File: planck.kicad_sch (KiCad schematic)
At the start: 142 parts, among them J1 USB_C_U262-161N-4BVC11, J2 USB_C_U262-161N-4BVC11, J3 USB_C_U262-161N-4BVC11, SW1 SW_Hotswap_Kailh_Choc_V1_1u, SW10 SW_Hotswap_Kailh_Choc_V1_1u, SW11 SW_Hotswap_Kailh_Choc_V1_1u, SW12 SW_Hotswap_Kailh_Choc_V1_1u, SW13 SW_Hotswap_Kailh_Choc_V1_1u, SW14 SW_Hotswap_Kailh_Choc_V1_1u, SW15 SW_Hotswap_Kailh_Choc_V1_1u, SW16 SW_Hotswap_Kailh_Choc_V1_1u, SW17 SW_Hotswap_Kailh_Choc_V1_1u, SW18 SW_Hotswap_Kailh_Choc_V1_1u, SW19 SW_Hotswap_Kailh_Choc_V1_1u, SW2 SW_Hotswap_Kailh_Choc_V1_1u, SW20 SW_Hotswap_Kailh_Choc_V1_1u, SW21 SW_Hotswap_Kailh_Choc_V1_1u, SW22 SW_Hotswap_Kailh_Choc_V1_1u, SW23 SW_Hotswap_Kailh_Choc_V1_1u, SW24 SW_Hotswap_Kailh_Choc_V1_1u, SW25 SW_Push, SW26 DSHP02TSGET, SW3 SW_Hotswap_Kailh_Choc_V1_1u, SW4 SW_Hotswap_Kailh_Choc_V1_1u, SW5 SW_Hotswap_Kailh_Choc_V1_1u, SW6 SW_Hotswap_Kailh_Choc_V1_1u, SW7 SW_Hotswap_Kailh_Choc_V1_1u, SW8 SW_Hotswap_Kailh_Choc_V1_1u, SW9 SW_Hotswap_Kailh_Choc_V1_1u, U1 RP2040 ARM Cortex-M0 133MHz, U2 ME6219C33M5G, U3 W25Q16JVUXIQ, U5 tcase, Y1 32MHz ±10ppm 20pF SMD3225-4P

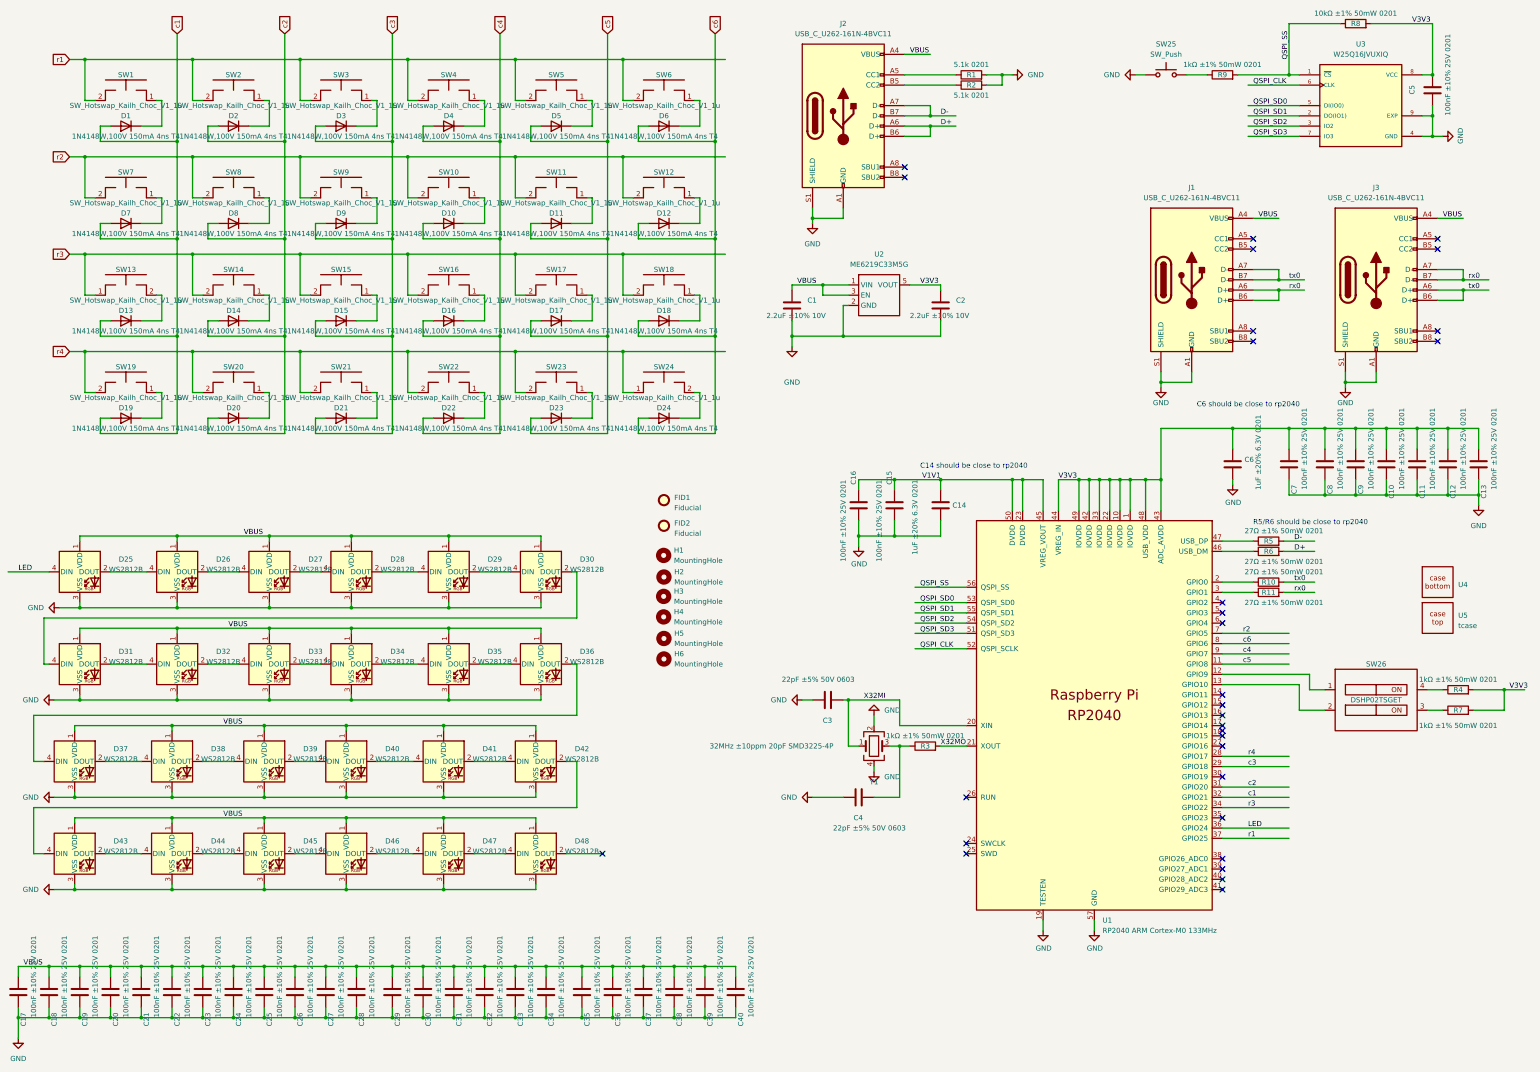
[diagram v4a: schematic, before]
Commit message: little  layout modification resistor over serial for protection  27R
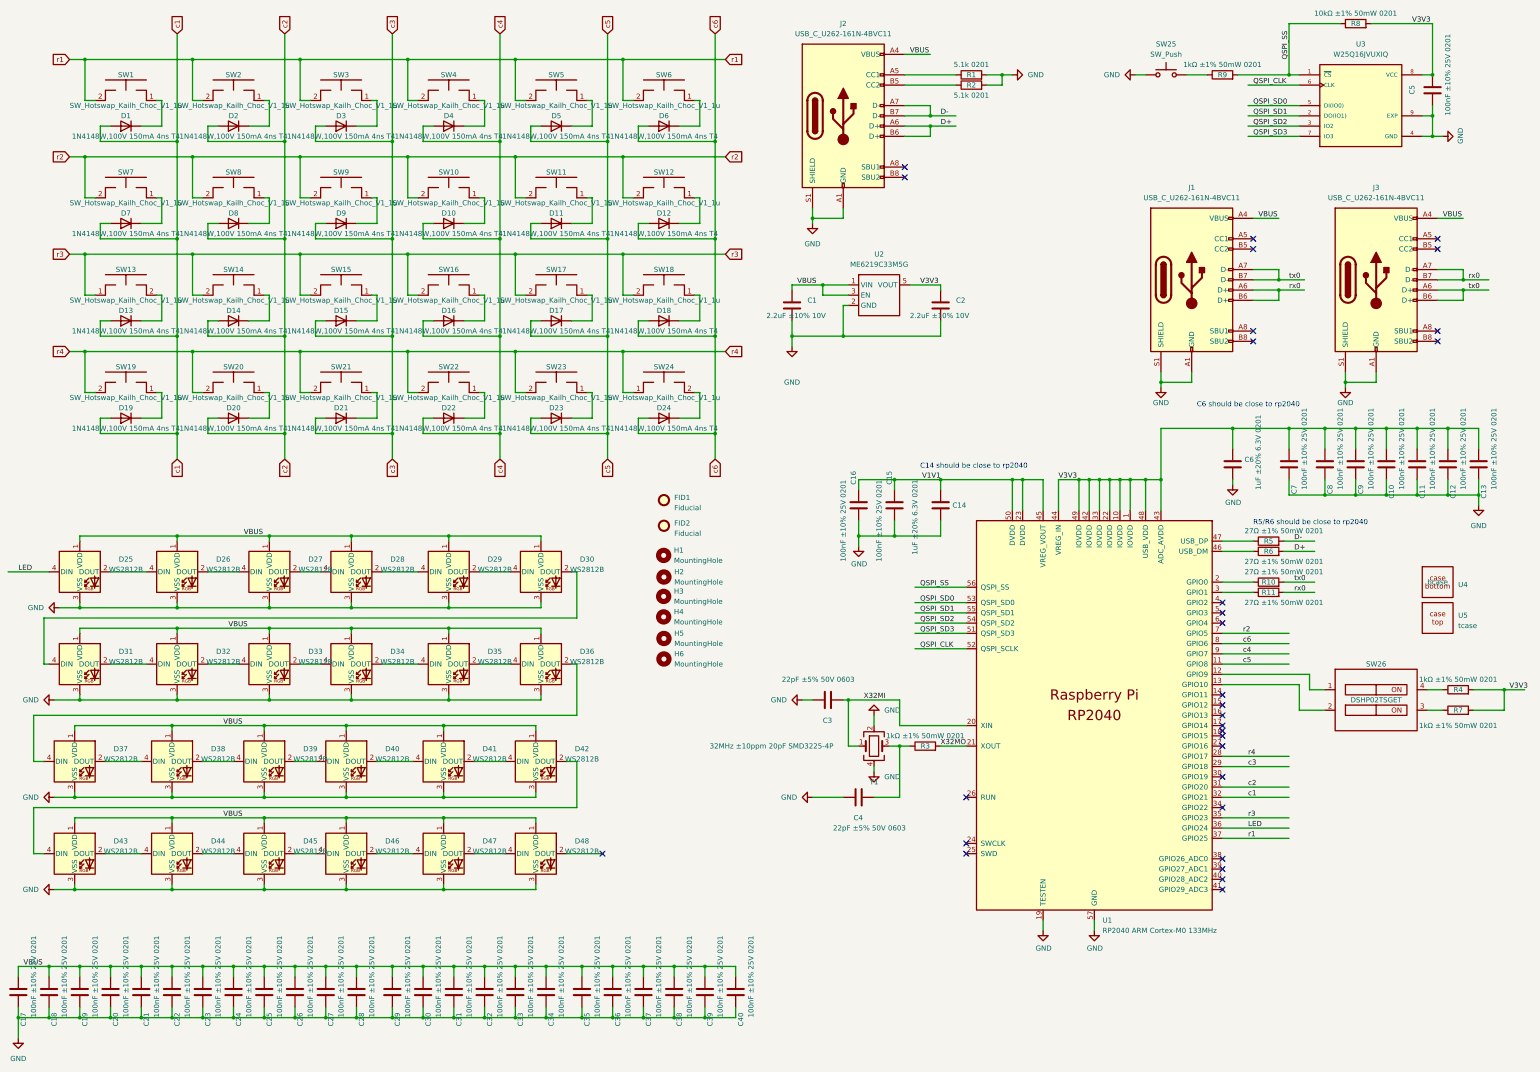
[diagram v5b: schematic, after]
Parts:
- J1, J2, J3: JLC C319148 -> C223907
- U4: value ~ -> bcase
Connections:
- net r3: now also U1.35 (GPIO23); no longer U1.34 (GPIO22)
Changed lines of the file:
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@@
   (junction (at 229.87 101.6) (diameter 0) (color 0 0 0 0)
   )
+  (junction (at 91.44 125.73) (diameter 0) (color 0 0 0 0)
+  )
   (junction (at 118.11 53.34) (diameter 0) (color 0 0 0 0)
   )
@@
   (junction (at 295.91 137.16) (diameter 0) (color 0 0 0 0)
   )
+  (junction (at 64.77 125.73) (diameter 0) (color 0 0 0 0)
+  )
   (junction (at 375.92 52.07) (diameter 0) (color 0 0 0 0)
   )
@@
   (junction (at 93.98 257.81) (diameter 0) (color 0 0 0 0)
   )
+  (junction (at 118.11 125.73) (diameter 0) (color 0 0 0 0)
+  )
   (junction (at 300.99 137.16) (diameter 0) (color 0 0 0 0)
   )
   (junction (at 106.68 215.9) (diameter 0) (color 0 0 0 0)
   )
+  (junction (at 144.78 125.73) (diameter 0) (color 0 0 0 0)
+  )
   (junction (at 87.63 168.91) (diameter 0) (color 0 0 0 0)
   )
@@
   (junction (at 71.12 257.81) (diameter 0) (color 0 0 0 0)
   )
+  (junction (at 171.45 125.73) (diameter 0) (color 0 0 0 0)
+  )
   (junction (at 132.08 151.13) (diameter 0) (color 0 0 0 0)
   )
   (junction (at 242.57 137.16) (diameter 0) (color 0 0 0 0)
   )
+  (junction (at 198.12 125.73) (diameter 0) (color 0 0 0 0)
+  )
   (junction (at 87.63 173.99) (diameter 0) (color 0 0 0 0)
   )
@@
   (no_connect (at 377.19 77.47))
   (no_connect (at 323.85 195.58))
+  (no_connect (at 323.85 218.44))
   (no_connect (at 323.85 190.5))
   (no_connect (at 331.47 100.33))
@@
   (no_connect (at 323.85 200.66))
   (no_connect (at 377.19 100.33))
-  (no_connect (at 323.85 220.98))
   (wire (pts (xy 55.88 73.66) (xy 60.96 73.66))
     (stroke (width 0) (type default))
@@
     (stroke (width 0) (type default))
   )
+  (wire (pts (xy 91.44 125.73) (xy 91.44 132.08))
+    (stroke (width 0) (type default))
+  )
   (wire (pts (xy 91.44 26.67) (xy 91.44 53.34))
     (stroke (width 0) (type default))
@@
     (stroke (width 0) (type default))
   )
+  (wire (pts (xy 198.12 125.73) (xy 198.12 132.08))
+    (stroke (width 0) (type default))
+  )
   (wire (pts (xy 74.93 73.66) (xy 72.39 73.66))
     (stroke (width 0) (type default))
@@
     (stroke (width 0) (type default))
   )
-  (wire (pts (xy 323.85 218.44) (xy 340.36 218.44))
+  (wire (pts (xy 323.85 220.98) (xy 340.36 220.98))
     (stroke (width 0) (type default))
   )
@@
     (stroke (width 0) (type default))
   )
+  (wire (pts (xy 118.11 125.73) (xy 118.11 132.08))
+    (stroke (width 0) (type default))
+  )
   (wire (pts (xy 140.97 270.51) (xy 148.59 270.51))
     (stroke (width 0) (type default))
@@
     (stroke (width 0) (type default))
   )
+  (wire (pts (xy 144.78 125.73) (xy 144.78 132.08))
+    (stroke (width 0) (type default))
+  )
   (wire (pts (xy 337.82 90.17) (xy 337.82 92.71))
     (stroke (width 0) (type default))
@@
     (stroke (width 0) (type default))
   )
+  (wire (pts (xy 171.45 125.73) (xy 171.45 132.08))
+    (stroke (width 0) (type default))
+  )
   (wire (pts (xy 156.21 270.51) (xy 156.21 267.97))
     (stroke (width 0) (type default))
@@
     (stroke (width 0) (type default))
   )
+  (wire (pts (xy 64.77 125.73) (xy 64.77 132.08))
+    (stroke (width 0) (type default))
+  )
   (wire (pts (xy 68.58 43.18) (xy 71.12 43.18))
     (stroke (width 0) (type default))
@@
     (effects (font (size 1.27 1.27)) (justify left bottom))
   )
-  (label "r3" (at 330.2 218.44 0) (fields_autoplaced)
+  (label "r3" (at 330.2 220.98 0) (fields_autoplaced)
     (effects (font (size 1.27 1.27)) (justify left bottom))
   )
@@
     )
   )
+  (global_label "r1" (shape input) (at 200.66 33.02 0) (fields_autoplaced)
+    (effects (font (size 1.27 1.27)) (justify left))
+    (property "Intersheetrefs" "${INTERSHEET_REFS}" (at 205.0688 32.9406 0)
+      (effects (font (size 1.27 1.27)) (justify left) hide)
+    )
+  )
   (global_label "r3" (shape input) (at 38.1 81.28 180) (fields_autoplaced)
     (effects (font (size 1.27 1.27)) (justify right))
@@
     )
   )
+  (global_label "c4" (shape input) (at 144.78 132.08 270) (fields_autoplaced)
+    (effects (font (size 1.27 1.27)) (justify right))
+    (property "Intersheetrefs" "${INTERSHEET_REFS}" (at 144.7006 136.7912 90)
+      (effects (font (size 1.27 1.27)) (justify left) hide)
+    )
+  )
+  (global_label "c6" (shape input) (at 198.12 132.08 270) (fields_autoplaced)
+    (effects (font (size 1.27 1.27)) (justify right))
+    (property "Intersheetrefs" "${INTERSHEET_REFS}" (at 198.0406 136.7912 90)
+      (effects (font (size 1.27 1.27)) (justify left) hide)
+    )
+  )
+  (global_label "r4" (shape input) (at 200.66 105.41 0) (fields_autoplaced)
+    (effects (font (size 1.27 1.27)) (justify left))
+    (property "Intersheetrefs" "${INTERSHEET_REFS}" (at 205.0688 105.3306 0)
+      (effects (font (size 1.27 1.27)) (justify left) hide)
+    )
+  )
   (global_label "c2" (shape input) (at 91.44 26.67 90) (fields_autoplaced)
     (effects (font (size 1.27 1.27)) (justify left))
@@
     )
   )
+  (global_label "r3" (shape input) (at 200.66 81.28 0) (fields_autoplaced)
+    (effects (font (size 1.27 1.27)) (justify left))
+    (property "Intersheetrefs" "${INTERSHEET_REFS}" (at 205.0688 81.2006 0)
+      (effects (font (size 1.27 1.27)) (justify left) hide)
+    )
+  )
+  (global_label "c2" (shape input) (at 91.44 132.08 270) (fields_autoplaced)
+    (effects (font (size 1.27 1.27)) (justify right))
+    (property "Intersheetrefs" "${INTERSHEET_REFS}" (at 91.3606 136.7912 90)
+      (effects (font (size 1.27 1.27)) (justify left) hide)
+    )
+  )
   (global_label "c4" (shape input) (at 144.78 26.67 90) (fields_autoplaced)
     (effects (font (size 1.27 1.27)) (justify left))
@@
     )
   )
+  (global_label "c1" (shape input) (at 64.77 132.08 270) (fields_autoplaced)
+    (effects (font (size 1.27 1.27)) (justify right))
+    (property "Intersheetrefs" "${INTERSHEET_REFS}" (at 64.6906 136.7912 90)
+      (effects (font (size 1.27 1.27)) (justify left) hide)
+    )
+  )
   (global_label "c1" (shape input) (at 64.77 26.67 90) (fields_autoplaced)
     (effects (font (size 1.27 1.27)) (justify left))
@@
     )
   )
+  (global_label "r2" (shape input) (at 200.66 57.15 0) (fields_autoplaced)
+    (effects (font (size 1.27 1.27)) (justify left))
+    (property "Intersheetrefs" "${INTERSHEET_REFS}" (at 205.0688 57.0706 0)
+      (effects (font (size 1.27 1.27)) (justify left) hide)
+    )
+  )
+  (global_label "c3" (shape input) (at 118.11 132.08 270) (fields_autoplaced)
+    (effects (font (size 1.27 1.27)) (justify right))
+    (property "Intersheetrefs" "${INTERSHEET_REFS}" (at 118.0306 136.7912 90)
+      (effects (font (size 1.27 1.27)) (justify left) hide)
+    )
+  )
+  (global_label "c5" (shape input) (at 171.45 132.08 270) (fields_autoplaced)
+    (effects (font (size 1.27 1.27)) (justify right))
+    (property "Intersheetrefs" "${INTERSHEET_REFS}" (at 171.3706 136.7912 90)
+      (effects (font (size 1.27 1.27)) (justify left) hide)
+    )
+  )
   (symbol (lib_id "Device:R") (at 356.87 24.13 90) (unit 1)
     (in_bom yes) (on_board yes) (dnp no)
@@
       (effects (font (size 1.27 1.27)) (justify left))
     )
-    (property "Value" "~" (at 377.19 162.56 0)
+    (property "Value" "bcase" (at 377.19 162.56 0)
       (effects (font (size 1.27 1.27)))
     )
@@
       (effects (font (size 1.27 1.27)) hide)
     )
-    (property "JLC" "C319148" (at 229.87 46.99 0)
+    (property "JLC" "C223907" (at 229.87 46.99 0)
       (effects (font (size 1.27 1.27)) hide)
     )
@@
       (effects (font (size 1.27 1.27)) hide)
     )
-    (property "JLC" "C319148" (at 361.95 87.63 0)
+    (property "JLC" "C223907" (at 361.95 87.63 0)
       (effects (font (size 1.27 1.27)) hide)
     )
@@
       (effects (font (size 1.27 1.27)) hide)
     )
-    (property "JLC" "C319148" (at 316.23 87.63 0)
+    (property "JLC" "C223907" (at 316.23 87.63 0)
       (effects (font (size 1.27 1.27)) hide)
     )
